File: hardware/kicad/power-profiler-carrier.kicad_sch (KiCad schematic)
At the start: 0 parts

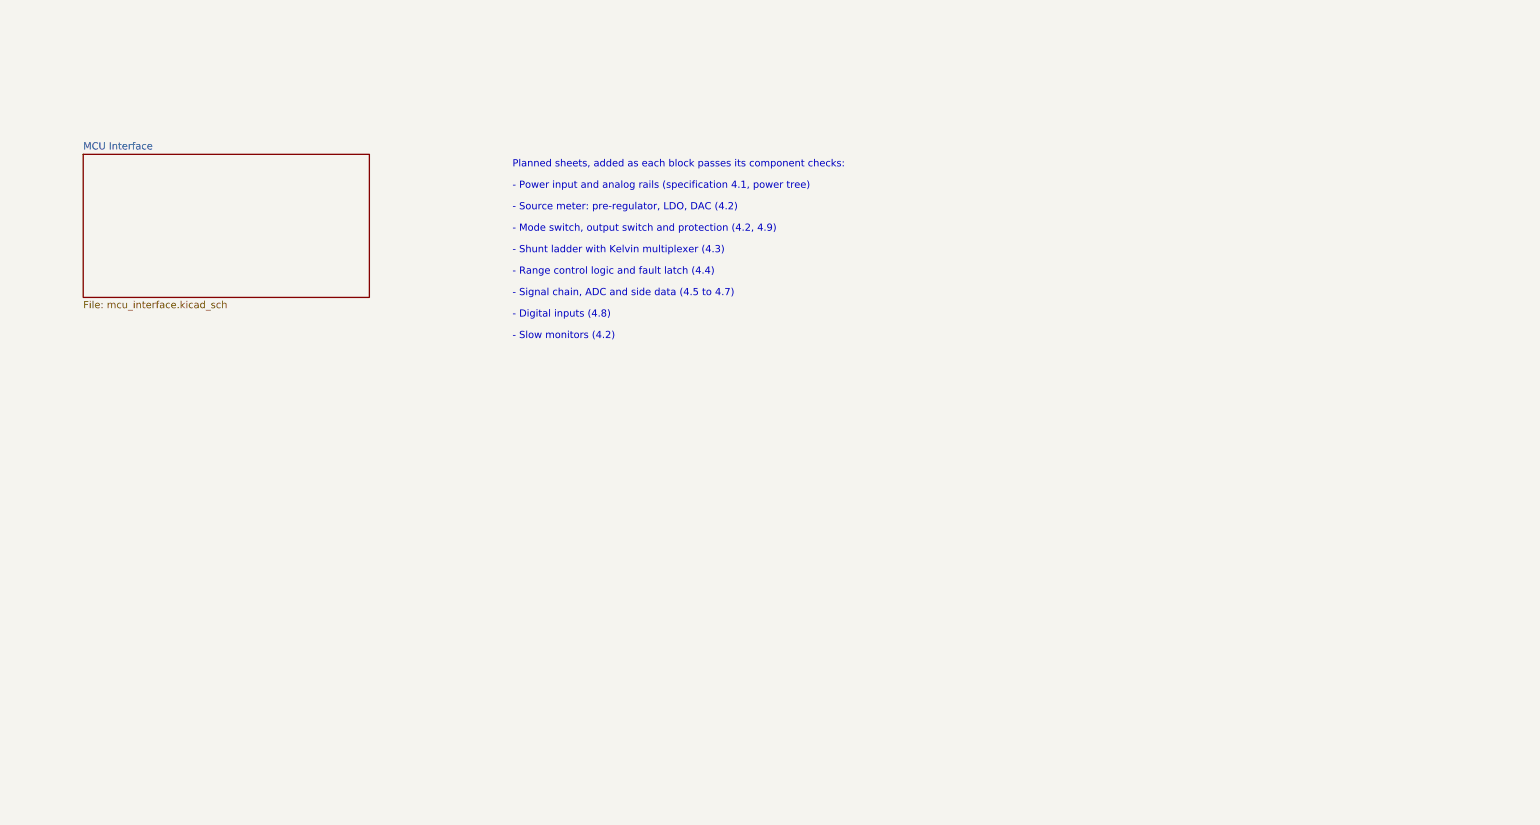
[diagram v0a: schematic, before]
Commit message: feat(hardware): draw the carrier board schematic as draft A0
Draw every block of the carrier board on thirteen A4 sheets: board
interface, power input, analog rails, source meter, path switching,
shunt ladder, output stage, signal chain, comparators, range logic,
digital inputs and monitors. Connections inside a sheet are wires,
supply rails use power symbols, and the root sheet joins the sheets
with wires between their hierarchical pins.

This is a review draft, drawn at the request of the project owner
before the component checks are closed. The parts are the candidates
of the specification, nothing was simulated or measured, and the logic
device that holds the range logic has no description yet.

The electrical rules check reports no errors and no warnings.
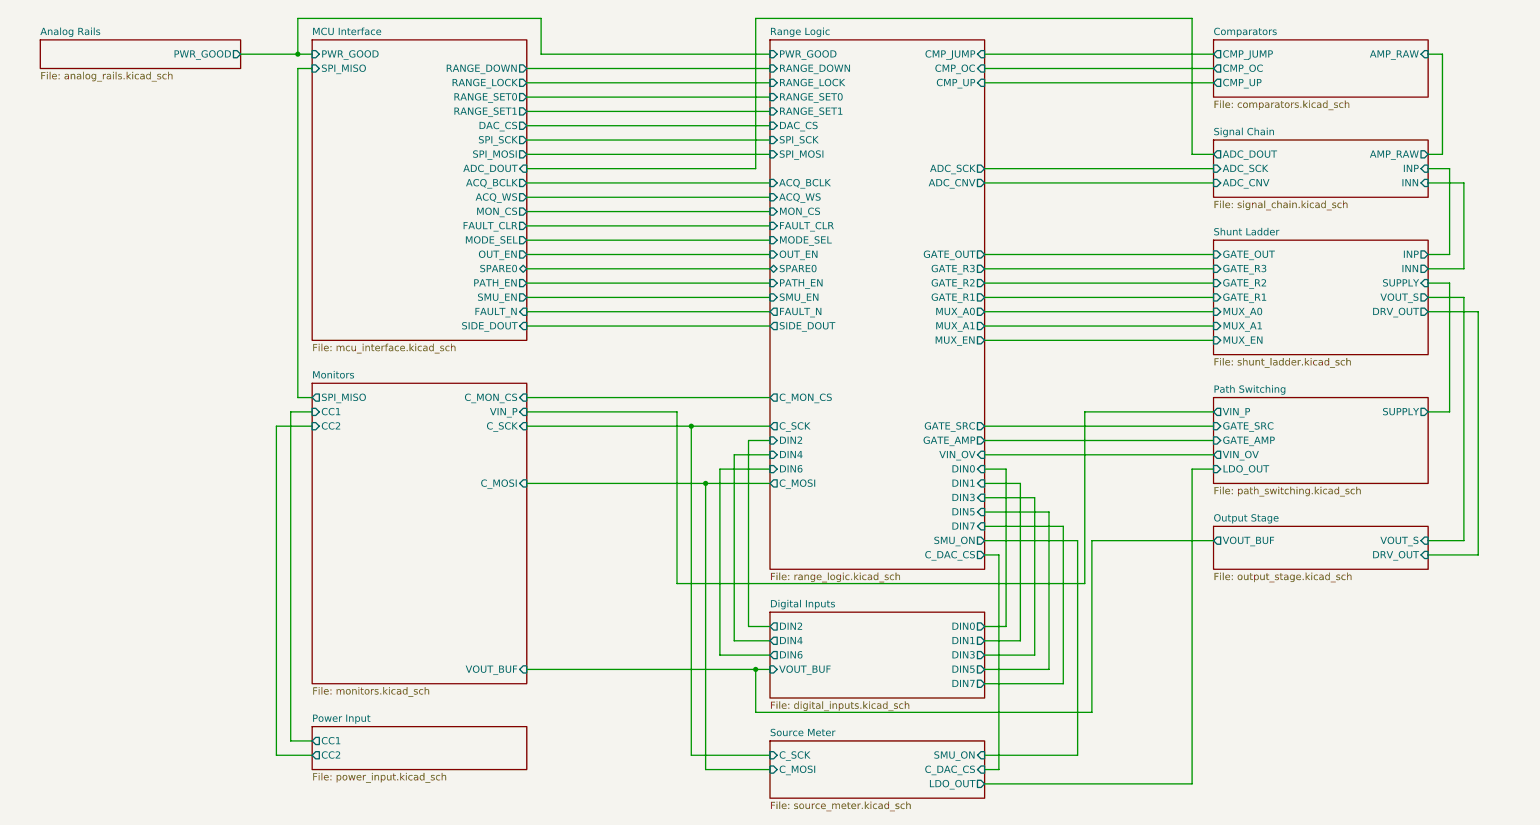
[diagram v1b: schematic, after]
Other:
- added sheet Analog Rails (analog_rails.kicad_sch)
- added sheet Comparators (comparators.kicad_sch)
- added sheet Digital Inputs (digital_inputs.kicad_sch)
- added sheet Monitors (monitors.kicad_sch)
- added sheet Output Stage (output_stage.kicad_sch)
- added sheet Path Switching (path_switching.kicad_sch)
- added sheet Power Input (power_input.kicad_sch)
- added sheet Range Logic (range_logic.kicad_sch)
- added sheet Shunt Ladder (shunt_ladder.kicad_sch)
- added sheet Signal Chain (signal_chain.kicad_sch)
- added sheet Source Meter (source_meter.kicad_sch)
- sheet MCU Interface ports: added ACQ_BCLK, ACQ_WS, ADC_DOUT, DAC_CS, FAULT_CLR, FAULT_N, MODE_SEL, MON_CS, OUT_EN, PATH_EN, PWR_GOOD, RANGE_DOWN, RANGE_LOCK, RANGE_SET0, RANGE_SET1, SIDE_DOUT, SMU_EN, SPARE0, SPI_MISO, SPI_MOSI, SPI_SCK; removed none
- note removed: "- Digital inputs (4.8)"
- note removed: "- Mode switch, output switch and protection (4.2, 4.9)"
- note removed: "- Power input and analog rails (specification 4.1, power tree)"
- note removed: "- Range control logic and fault latch (4.4)"
- note removed: "- Shunt ladder with Kelvin multiplexer (4.3)"
- note removed: "- Signal chain, ADC and side data (4.5 to 4.7)"
- note removed: "- Slow monitors (4.2)"
- note removed: "- Source meter: pre-regulator, LDO, DAC (4.2)"
- note removed: "Planned sheets, added as each block passes its component checks:"
- title: Power Profiler Carrier -> ESP32-S3 Power Profiler - Carrier Board

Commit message: feat(hardware)!: draw draft A1 of the schematic around a Pico 2
A Raspberry Pi Pico 2 on two 1x20 sockets replaces the ESP32-S3
development board, the programmable logic device and the buffer
between the two boards (D-39 to D-43 of the specification). The former
interface and range logic sheets become two new ones:

- Controller: the Pico 2, the diodes that join its USB supply and the
  5 V rail of the carrier, resistor arrays in the SPI and acquisition
  lines, a reset button and a console header.
- Side Data: two shift registers that take the range, the status
  signals and the eight logic inputs with every sample.

The DUT connects through a 1x4 pin header and a lever terminal block
in parallel, both GND, VIN, VOUT, GND, and the logic port is a 1x10
header with VCC, GND, D7 to D0: the pin order of the PPK2 (D-44). A
solder jumper selects the supply of the DUT side of the level
translator. A transistor at the driver of the ampere switch holds it
open while VIN is above 5.5 V.

Reference designators are numbered as the annotation tool of KiCad
does by default (D-45). The numbering touches every sheet, so these
changes come in one commit. The symbol and the socket footprint of
the ESP32-S3 board leave the project library; the Pico 2 uses the
symbol and the footprint of the KiCad library.

The electrical rules check reports no errors and no warnings. The
parts stay candidates, and no program for the PIO blocks exists yet.

BREAKING CHANGE: the pins of the controller follow the new pin map of
section 5 of the specification.
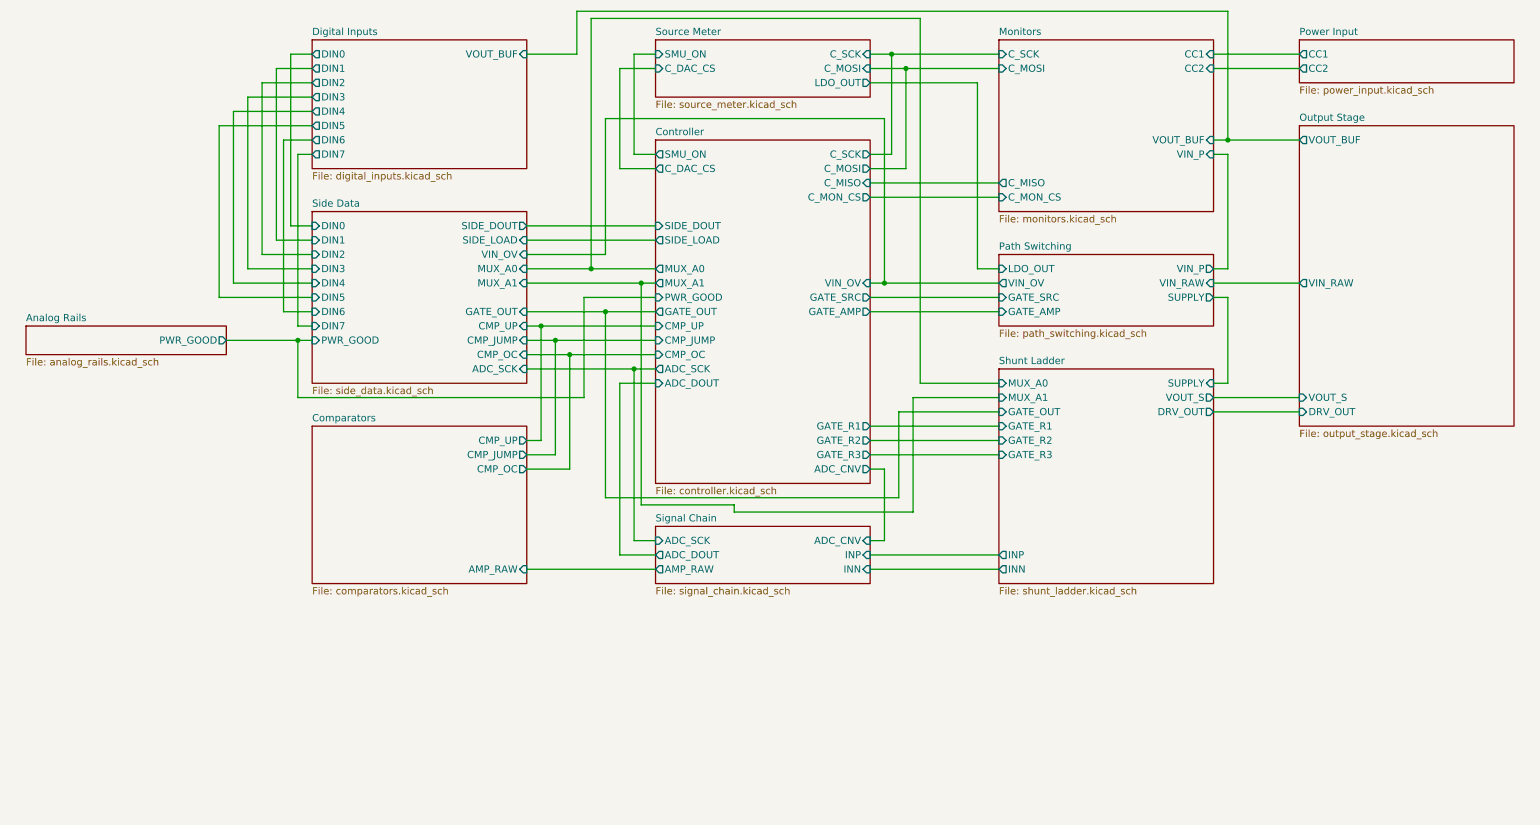
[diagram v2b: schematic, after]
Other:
- sheet MCU Interface renamed Controller
- removed sheet Range Logic
- added sheet Side Data (side_data.kicad_sch)
- sheet Controller: file mcu_interface.kicad_sch -> controller.kicad_sch
- sheet Controller ports: added ADC_CNV, ADC_SCK, CMP_JUMP, CMP_OC, CMP_UP, C_DAC_CS, C_MISO, C_MON_CS, C_MOSI, C_SCK, GATE_AMP, GATE_OUT, GATE_R1, GATE_R2, GATE_R3, GATE_SRC, MUX_A0, MUX_A1, SIDE_LOAD, SMU_ON, VIN_OV; removed ACQ_BCLK, ACQ_WS, DAC_CS, FAULT_CLR, FAULT_N, MODE_SEL, MON_CS, OUT_EN, PATH_EN, RANGE_DOWN, RANGE_LOCK, RANGE_SET0, RANGE_SET1, SMU_EN, SPARE0, SPI_MISO, SPI_MOSI, SPI_SCK
- sheet Monitors ports: added C_MISO; removed SPI_MISO
- sheet Output Stage ports: added VIN_RAW; removed none
- sheet Path Switching ports: added VIN_RAW; removed none
- sheet Shunt Ladder ports: added none; removed MUX_EN
- title: ESP32-S3 Power Profiler - Carrier Board -> Power Profiler - Carrier Board

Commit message: feat(hardware): draw draft A2 of the schematic
428 parts on 15 A4 pages, 14 sheets below the root sheet (D-83). Two
sheets are new: Logic Supplies, with the supervisor of the 5 V rail and
the two 3.3 V regulators, and Rail Monitor, with the comparators behind
PWR_GOOD.

The drawings follow the specification of draft A2: a current limiter
on each supply input and a priority multiplexer, a pre-regulator that
tracks the output of the linear regulator, a VIN path that withstands
-20 V to +20 V with its switch open, two diode-connected MOSFETs as
ladder clamp, thin-film and four-terminal shunts, ESD arrays at the CC
pins and at the VCC pin of the logic port. The reference designators
are numbered as KiCad numbers them (D-45), so they are not those of
draft A1.

The project library gains the symbol of the input multiplexer and two
footprints: the lever terminal block with pads of 1.9 mm x 2.3 mm and
the controller module without its antenna keep-out (D-85).

The electrical rules check reports no errors and no warnings. The
parts are candidates, and nothing is built or measured.
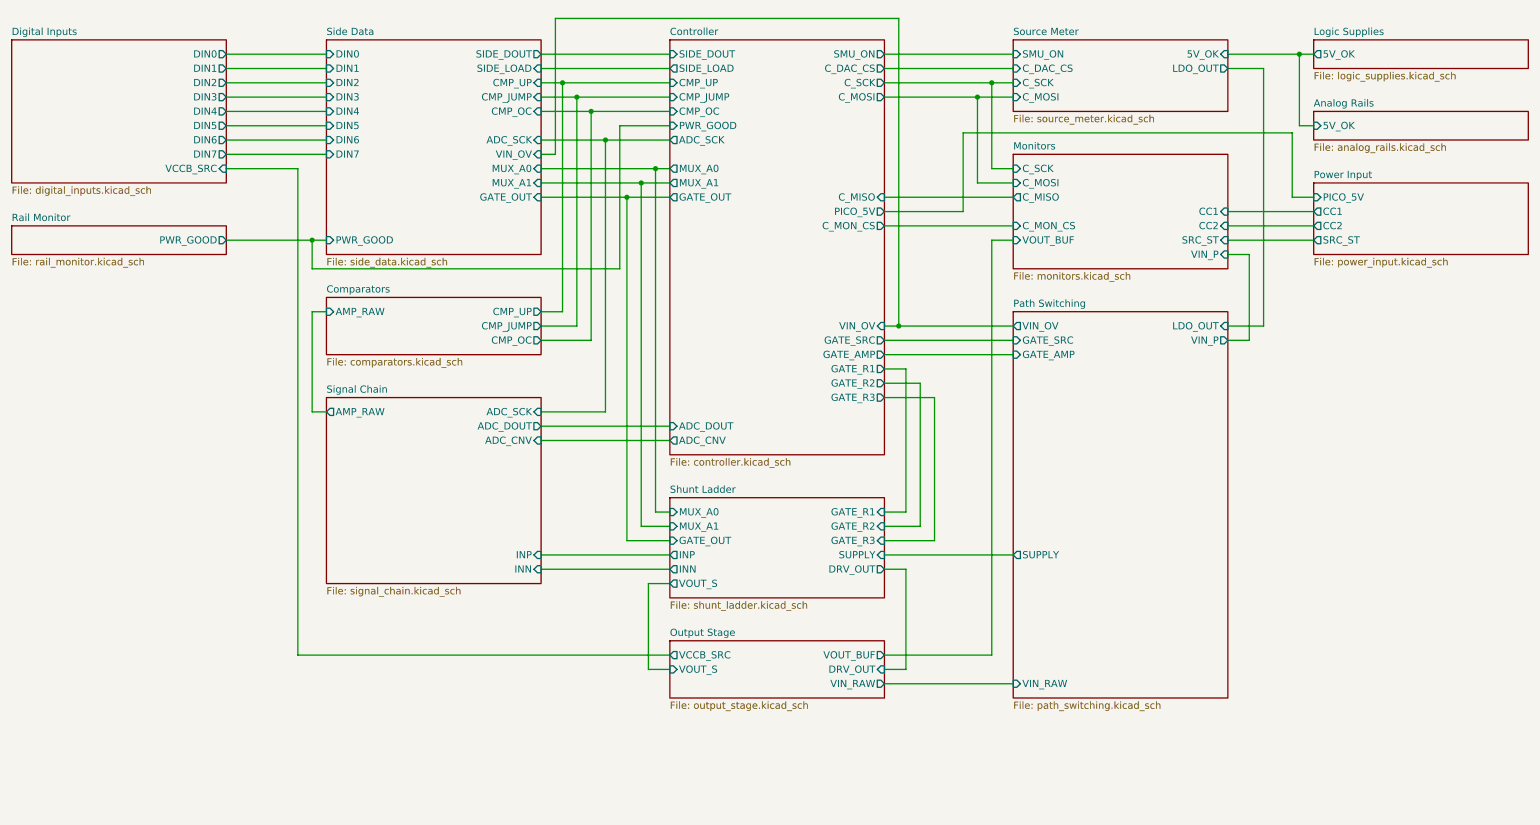
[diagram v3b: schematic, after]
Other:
- added sheet Logic Supplies (logic_supplies.kicad_sch)
- added sheet Rail Monitor (rail_monitor.kicad_sch)
- sheet Analog Rails ports: added 5V_OK; removed PWR_GOOD
- sheet Controller ports: added PICO_5V; removed none
- sheet Digital Inputs ports: added VCCB_SRC; removed VOUT_BUF
- sheet Monitors ports: added SRC_ST; removed none
- sheet Output Stage ports: added VCCB_SRC; removed none
- sheet Power Input ports: added PICO_5V, SRC_ST; removed none
- sheet Source Meter ports: added 5V_OK; removed none

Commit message: docs(hardware): name the project in the schematic title block
The title block of the root page now reads "Open Power Profiler -
Carrier Board", as the silkscreen and the title block of the board do
since the previous commit. The circuit is unchanged: the electrical
rules check reports no error and no warning, and the board still
agrees with the schematic.

The schematic PDF and the picture of its root page are exported again
with KiCad set to English. The other 14 pages are the same as before,
compared page by page.
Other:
- title: Power Profiler - Carrier Board -> Open Power Profiler - Carrier Board
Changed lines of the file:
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@@
 	(paper "A4")
 	(title_block
-		(title "Power Profiler - Carrier Board")
+		(title "Open Power Profiler - Carrier Board")
 		(date "2026-10-09")
 		(rev "A2 (draft)")
